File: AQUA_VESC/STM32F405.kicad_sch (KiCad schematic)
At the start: 15 parts, among them J3 Conn_01x05_Pin, U4 STM32F405RGTx, X1 8MHz

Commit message: AQUA VESC仮完成
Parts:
- renumbered U4 to U3
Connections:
- net ADC_EXT2 renamed MISO_ADC_EXT2
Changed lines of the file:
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@@
 		)
 	)
-	(hierarchical_label "ADC_EXT2"
+	(hierarchical_label "MISO_ADC_EXT2"
 		(shape output)
 		(at 80.01 53.34 0)
@@
 		(dnp no)
 		(fields_autoplaced yes)
-		(property "Reference" "#PWR029"
+		(property "Reference" "#PWR025"
 			(at 22.86 39.37 0)
 			(effects
@@
 			(project "AQUA_VESC"
 				(path "/8ee9fd02-9bd5-4905-927f-d8ca1179f479/d65f5897-766b-4e01-8d8f-d620c6f94f16"
-					(reference "#PWR029")
+					(reference "#PWR025")
 					(unit 1)
 				)
@@
 		(dnp no)
 		(fields_autoplaced yes)
-		(property "Reference" "#PWR031"
+		(property "Reference" "#PWR027"
 			(at 26.67 125.73 0)
 			(effects
@@
 			(project "AQUA_VESC"
 				(path "/8ee9fd02-9bd5-4905-927f-d8ca1179f479/d65f5897-766b-4e01-8d8f-d620c6f94f16"
-					(reference "#PWR031")
+					(reference "#PWR027")
 					(unit 1)
 				)
@@
 		(dnp no)
 		(fields_autoplaced yes)
-		(property "Reference" "#PWR036"
+		(property "Reference" "#PWR032"
 			(at 82.55 36.83 0)
 			(effects
@@
 			(project "AQUA_VESC"
 				(path "/8ee9fd02-9bd5-4905-927f-d8ca1179f479/d65f5897-766b-4e01-8d8f-d620c6f94f16"
-					(reference "#PWR036")
+					(reference "#PWR032")
 					(unit 1)
 				)
@@
 		(dnp no)
 		(fields_autoplaced yes)
-		(property "Reference" "#PWR030"
+		(property "Reference" "#PWR026"
 			(at 22.86 45.72 0)
 			(effects
@@
 			(project "AQUA_VESC"
 				(path "/8ee9fd02-9bd5-4905-927f-d8ca1179f479/d65f5897-766b-4e01-8d8f-d620c6f94f16"
-					(reference "#PWR030")
+					(reference "#PWR026")
 					(unit 1)
 				)
@@
 		(dnp no)
 		(fields_autoplaced yes)
-		(property "Reference" "#PWR038"
+		(property "Reference" "#PWR034"
 			(at 118.11 38.1 0)
 			(effects
@@
 			(project "AQUA_VESC"
 				(path "/8ee9fd02-9bd5-4905-927f-d8ca1179f479/d65f5897-766b-4e01-8d8f-d620c6f94f16"
-					(reference "#PWR038")
+					(reference "#PWR034")
 					(unit 1)
 				)
@@
 		(dnp no)
 		(fields_autoplaced yes)
-		(property "Reference" "U4"
+		(property "Reference" "U3"
 			(at 64.3733 127 0)
 			(effects
@@
 			(project ""
 				(path "/8ee9fd02-9bd5-4905-927f-d8ca1179f479/d65f5897-766b-4e01-8d8f-d620c6f94f16"
-					(reference "U4")
+					(reference "U3")
 					(unit 1)
 				)
@@
 		(dnp no)
 		(fields_autoplaced yes)
-		(property "Reference" "#PWR035"
+		(property "Reference" "#PWR031"
 			(at 67.31 22.86 0)
 			(effects
@@
 			(project ""
 				(path "/8ee9fd02-9bd5-4905-927f-d8ca1179f479/d65f5897-766b-4e01-8d8f-d620c6f94f16"
-					(reference "#PWR035")
+					(reference "#PWR031")
 					(unit 1)
 				)
@@
 		(dnp no)
 		(fields_autoplaced yes)
-		(property "Reference" "#PWR037"
+		(property "Reference" "#PWR033"
 			(at 120.65 33.02 0)
 			(effects
@@
 			(project "AQUA_VESC"
 				(path "/8ee9fd02-9bd5-4905-927f-d8ca1179f479/d65f5897-766b-4e01-8d8f-d620c6f94f16"
-					(reference "#PWR037")
+					(reference "#PWR033")
 					(unit 1)
 				)
@@
 		(dnp no)
 		(fields_autoplaced yes)
-		(property "Reference" "#PWR032"
+		(property "Reference" "#PWR028"
 			(at 27.94 67.31 0)
 			(effects
@@
 			(project "AQUA_VESC"
 				(path "/8ee9fd02-9bd5-4905-927f-d8ca1179f479/d65f5897-766b-4e01-8d8f-d620c6f94f16"
-					(reference "#PWR032")
+					(reference "#PWR028")
 					(unit 1)
 				)
@@
 		(dnp no)
 		(fields_autoplaced yes)
-		(property "Reference" "#PWR027"
+		(property "Reference" "#PWR023"
 			(at 17.78 67.31 0)
 			(effects
@@
 			(project "AQUA_VESC"
 				(path "/8ee9fd02-9bd5-4905-927f-d8ca1179f479/d65f5897-766b-4e01-8d8f-d620c6f94f16"
-					(reference "#PWR027")
+					(reference "#PWR023")
 					(unit 1)
 				)
@@
 		(dnp no)
 		(fields_autoplaced yes)
-		(property "Reference" "#PWR033"
+		(property "Reference" "#PWR029"
 			(at 31.75 49.53 0)
 			(effects
@@
 			(project "AQUA_VESC"
 				(path "/8ee9fd02-9bd5-4905-927f-d8ca1179f479/d65f5897-766b-4e01-8d8f-d620c6f94f16"
-					(reference "#PWR033")
+					(reference "#PWR029")
 					(unit 1)
 				)
@@
 		(dnp no)
 		(fields_autoplaced yes)
-		(property "Reference" "#PWR034"
+		(property "Reference" "#PWR030"
 			(at 59.69 135.89 0)
 			(effects
@@
 			(project ""
 				(path "/8ee9fd02-9bd5-4905-927f-d8ca1179f479/d65f5897-766b-4e01-8d8f-d620c6f94f16"
-					(reference "#PWR034")
+					(reference "#PWR030")
 					(unit 1)
 				)
@@
 		(dnp no)
 		(fields_autoplaced yes)
-		(property "Reference" "#PWR028"
+		(property "Reference" "#PWR024"
 			(at 22.86 22.86 0)
 			(effects
@@
 			(project "AQUA_VESC"
 				(path "/8ee9fd02-9bd5-4905-927f-d8ca1179f479/d65f5897-766b-4e01-8d8f-d620c6f94f16"
-					(reference "#PWR028")
-					(unit 1)
-				)
+					(reference "#PWR024")
+					(unit 1)
+				)

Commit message: 制御基板REV01完成
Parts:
- renumbered J3 to J2
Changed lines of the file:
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@@
 		(dnp no)
 		(fields_autoplaced yes)
-		(property "Reference" "#PWR025"
+		(property "Reference" "#PWR024"
 			(at 22.86 39.37 0)
 			(effects
@@
 			(project "AQUA_VESC"
 				(path "/8ee9fd02-9bd5-4905-927f-d8ca1179f479/d65f5897-766b-4e01-8d8f-d620c6f94f16"
-					(reference "#PWR025")
+					(reference "#PWR024")
 					(unit 1)
 				)
@@
 		(dnp no)
 		(fields_autoplaced yes)
-		(property "Reference" "J3"
+		(property "Reference" "J2"
 			(at 134.62 36.8299 0)
 			(effects
@@
 			(project ""
 				(path "/8ee9fd02-9bd5-4905-927f-d8ca1179f479/d65f5897-766b-4e01-8d8f-d620c6f94f16"
-					(reference "J3")
+					(reference "J2")
 					(unit 1)
 				)
@@
 		(dnp no)
 		(fields_autoplaced yes)
-		(property "Reference" "#PWR027"
+		(property "Reference" "#PWR026"
 			(at 26.67 125.73 0)
 			(effects
@@
 			(project "AQUA_VESC"
 				(path "/8ee9fd02-9bd5-4905-927f-d8ca1179f479/d65f5897-766b-4e01-8d8f-d620c6f94f16"
-					(reference "#PWR027")
+					(reference "#PWR026")
 					(unit 1)
 				)
@@
 		(dnp no)
 		(fields_autoplaced yes)
-		(property "Reference" "#PWR032"
+		(property "Reference" "#PWR031"
 			(at 82.55 36.83 0)
 			(effects
@@
 			(project "AQUA_VESC"
 				(path "/8ee9fd02-9bd5-4905-927f-d8ca1179f479/d65f5897-766b-4e01-8d8f-d620c6f94f16"
-					(reference "#PWR032")
+					(reference "#PWR031")
 					(unit 1)
 				)
@@
 		(dnp no)
 		(fields_autoplaced yes)
-		(property "Reference" "#PWR026"
+		(property "Reference" "#PWR025"
 			(at 22.86 45.72 0)
 			(effects
@@
 			(project "AQUA_VESC"
 				(path "/8ee9fd02-9bd5-4905-927f-d8ca1179f479/d65f5897-766b-4e01-8d8f-d620c6f94f16"
-					(reference "#PWR026")
+					(reference "#PWR025")
 					(unit 1)
 				)
@@
 		(dnp no)
 		(fields_autoplaced yes)
-		(property "Reference" "#PWR034"
+		(property "Reference" "#PWR033"
 			(at 118.11 38.1 0)
 			(effects
@@
 			(project "AQUA_VESC"
 				(path "/8ee9fd02-9bd5-4905-927f-d8ca1179f479/d65f5897-766b-4e01-8d8f-d620c6f94f16"
-					(reference "#PWR034")
+					(reference "#PWR033")
 					(unit 1)
 				)
@@
 		(dnp no)
 		(fields_autoplaced yes)
-		(property "Reference" "#PWR031"
+		(property "Reference" "#PWR030"
 			(at 67.31 22.86 0)
 			(effects
@@
 			(project ""
 				(path "/8ee9fd02-9bd5-4905-927f-d8ca1179f479/d65f5897-766b-4e01-8d8f-d620c6f94f16"
-					(reference "#PWR031")
+					(reference "#PWR030")
 					(unit 1)
 				)
@@
 		(dnp no)
 		(fields_autoplaced yes)
-		(property "Reference" "#PWR033"
+		(property "Reference" "#PWR032"
 			(at 120.65 33.02 0)
 			(effects
@@
 			(project "AQUA_VESC"
 				(path "/8ee9fd02-9bd5-4905-927f-d8ca1179f479/d65f5897-766b-4e01-8d8f-d620c6f94f16"
-					(reference "#PWR033")
+					(reference "#PWR032")
 					(unit 1)
 				)
@@
 		(dnp no)
 		(fields_autoplaced yes)
-		(property "Reference" "#PWR028"
+		(property "Reference" "#PWR027"
 			(at 27.94 67.31 0)
 			(effects
@@
 			(project "AQUA_VESC"
 				(path "/8ee9fd02-9bd5-4905-927f-d8ca1179f479/d65f5897-766b-4e01-8d8f-d620c6f94f16"
-					(reference "#PWR028")
+					(reference "#PWR027")
 					(unit 1)
 				)
@@
 		(dnp no)
 		(fields_autoplaced yes)
-		(property "Reference" "#PWR023"
+		(property "Reference" "#PWR022"
 			(at 17.78 67.31 0)
 			(effects
@@
 			(project "AQUA_VESC"
 				(path "/8ee9fd02-9bd5-4905-927f-d8ca1179f479/d65f5897-766b-4e01-8d8f-d620c6f94f16"
-					(reference "#PWR023")
+					(reference "#PWR022")
 					(unit 1)
 				)
@@
 		(dnp no)
 		(fields_autoplaced yes)
-		(property "Reference" "#PWR029"
+		(property "Reference" "#PWR028"
 			(at 31.75 49.53 0)
 			(effects
@@
 			(project "AQUA_VESC"
 				(path "/8ee9fd02-9bd5-4905-927f-d8ca1179f479/d65f5897-766b-4e01-8d8f-d620c6f94f16"
-					(reference "#PWR029")
+					(reference "#PWR028")
 					(unit 1)
 				)
@@
 		(dnp no)
 		(fields_autoplaced yes)
-		(property "Reference" "#PWR030"
+		(property "Reference" "#PWR029"
 			(at 59.69 135.89 0)
 			(effects
@@
 			(project ""
 				(path "/8ee9fd02-9bd5-4905-927f-d8ca1179f479/d65f5897-766b-4e01-8d8f-d620c6f94f16"
-					(reference "#PWR030")
+					(reference "#PWR029")
 					(unit 1)
 				)
@@
 		(dnp no)
 		(fields_autoplaced yes)
-		(property "Reference" "#PWR024"
+		(property "Reference" "#PWR023"
 			(at 22.86 22.86 0)
 			(effects
@@
 			(project "AQUA_VESC"
 				(path "/8ee9fd02-9bd5-4905-927f-d8ca1179f479/d65f5897-766b-4e01-8d8f-d620c6f94f16"
-					(reference "#PWR024")
-					(unit 1)
-				)
+					(reference "#PWR023")
+					(unit 1)
+				)

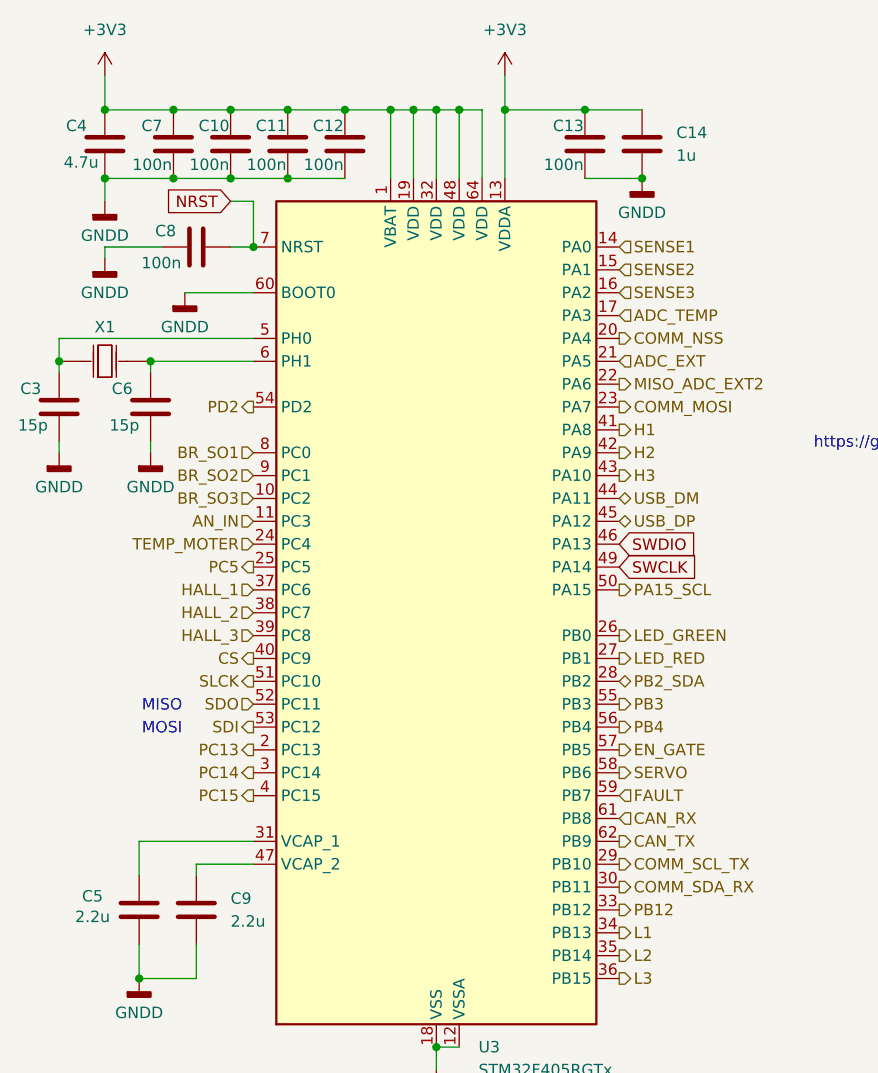
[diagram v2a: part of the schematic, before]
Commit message: 方針変更、back_connector_escにMT60を使用しないことに
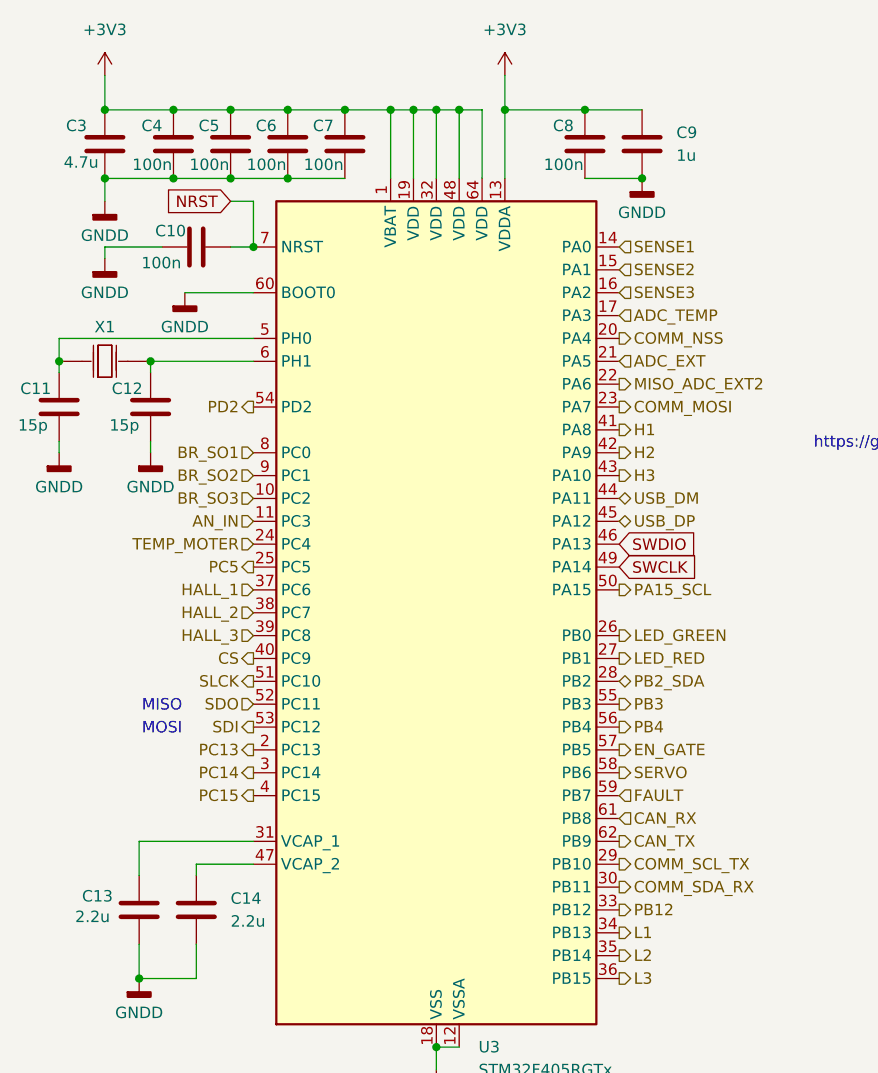
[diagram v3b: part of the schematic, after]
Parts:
- renumbered C8 to C10, C3 to C11, C6 to C12, C5 to C13, C9 to C14, C4 to C3, C7 to C4, C10 to C5, C11 to C6, C12 to C7, C13 to C8, C14 to C9
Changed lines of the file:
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@@
 		(dnp no)
 		(fields_autoplaced yes)
-		(property "Reference" "#PWR024"
+		(property "Reference" "#PWR032"
 			(at 22.86 39.37 0)
 			(effects
@@
 			(project "AQUA_VESC"
 				(path "/8ee9fd02-9bd5-4905-927f-d8ca1179f479/d65f5897-766b-4e01-8d8f-d620c6f94f16"
-					(reference "#PWR024")
+					(reference "#PWR032")
 					(unit 1)
 				)
@@
 		(on_board yes)
 		(dnp no)
-		(property "Reference" "C13"
+		(property "Reference" "C8"
 			(at 72.644 24.638 0)
 			(effects
@@
 			(project "AQUA_VESC"
 				(path "/8ee9fd02-9bd5-4905-927f-d8ca1179f479/d65f5897-766b-4e01-8d8f-d620c6f94f16"
-					(reference "C13")
+					(reference "C8")
 					(unit 1)
 				)
@@
 		(on_board yes)
 		(dnp no)
-		(property "Reference" "C8"
+		(property "Reference" "C10"
 			(at 28.448 36.322 90)
 			(effects
@@
 			(project ""
 				(path "/8ee9fd02-9bd5-4905-927f-d8ca1179f479/d65f5897-766b-4e01-8d8f-d620c6f94f16"
-					(reference "C8")
+					(reference "C10")
 					(unit 1)
 				)
@@
 		(on_board yes)
 		(dnp no)
-		(property "Reference" "C11"
+		(property "Reference" "C6"
 			(at 39.624 24.638 0)
 			(effects
@@
 			(project "AQUA_VESC"
 				(path "/8ee9fd02-9bd5-4905-927f-d8ca1179f479/d65f5897-766b-4e01-8d8f-d620c6f94f16"
-					(reference "C11")
+					(reference "C6")
 					(unit 1)
 				)
@@
 		(dnp no)
 		(fields_autoplaced yes)
-		(property "Reference" "#PWR026"
+		(property "Reference" "#PWR038"
 			(at 26.67 125.73 0)
 			(effects
@@
 			(project "AQUA_VESC"
 				(path "/8ee9fd02-9bd5-4905-927f-d8ca1179f479/d65f5897-766b-4e01-8d8f-d620c6f94f16"
-					(reference "#PWR026")
+					(reference "#PWR038")
 					(unit 1)
 				)
@@
 		(dnp no)
 		(fields_autoplaced yes)
-		(property "Reference" "#PWR025"
+		(property "Reference" "#PWR034"
 			(at 22.86 45.72 0)
 			(effects
@@
 			(project "AQUA_VESC"
 				(path "/8ee9fd02-9bd5-4905-927f-d8ca1179f479/d65f5897-766b-4e01-8d8f-d620c6f94f16"
-					(reference "#PWR025")
+					(reference "#PWR034")
 					(unit 1)
 				)
@@
 		(on_board yes)
 		(dnp no)
-		(property "Reference" "C10"
+		(property "Reference" "C5"
 			(at 33.274 24.638 0)
 			(effects
@@
 			(project "AQUA_VESC"
 				(path "/8ee9fd02-9bd5-4905-927f-d8ca1179f479/d65f5897-766b-4e01-8d8f-d620c6f94f16"
-					(reference "C10")
+					(reference "C5")
 					(unit 1)
 				)
@@
 		(dnp no)
 		(fields_autoplaced yes)
-		(property "Reference" "#PWR030"
+		(property "Reference" "#PWR029"
 			(at 67.31 22.86 0)
 			(effects
@@
 			(project ""
 				(path "/8ee9fd02-9bd5-4905-927f-d8ca1179f479/d65f5897-766b-4e01-8d8f-d620c6f94f16"
-					(reference "#PWR030")
+					(reference "#PWR029")
 					(unit 1)
 				)
@@
 		(on_board yes)
 		(dnp no)
-		(property "Reference" "C7"
+		(property "Reference" "C4"
 			(at 26.924 24.638 0)
 			(effects
@@
 			(project "AQUA_VESC"
 				(path "/8ee9fd02-9bd5-4905-927f-d8ca1179f479/d65f5897-766b-4e01-8d8f-d620c6f94f16"
-					(reference "C7")
+					(reference "C4")
 					(unit 1)
 				)
@@
 		(dnp no)
 		(fields_autoplaced yes)
-		(property "Reference" "#PWR032"
+		(property "Reference" "#PWR030"
 			(at 120.65 33.02 0)
 			(effects
@@
 			(project "AQUA_VESC"
 				(path "/8ee9fd02-9bd5-4905-927f-d8ca1179f479/d65f5897-766b-4e01-8d8f-d620c6f94f16"
-					(reference "#PWR032")
+					(reference "#PWR030")
 					(unit 1)
 				)
@@
 		(dnp no)
 		(fields_autoplaced yes)
-		(property "Reference" "#PWR027"
+		(property "Reference" "#PWR037"
 			(at 27.94 67.31 0)
 			(effects
@@
 			(project "AQUA_VESC"
 				(path "/8ee9fd02-9bd5-4905-927f-d8ca1179f479/d65f5897-766b-4e01-8d8f-d620c6f94f16"
-					(reference "#PWR027")
+					(reference "#PWR037")
 					(unit 1)
 				)
@@
 		(dnp no)
 		(fields_autoplaced yes)
-		(property "Reference" "#PWR022"
+		(property "Reference" "#PWR036"
 			(at 17.78 67.31 0)
 			(effects
@@
 			(project "AQUA_VESC"
 				(path "/8ee9fd02-9bd5-4905-927f-d8ca1179f479/d65f5897-766b-4e01-8d8f-d620c6f94f16"
-					(reference "#PWR022")
+					(reference "#PWR036")
 					(unit 1)
 				)
@@
 		(on_board yes)
 		(dnp no)
-		(property "Reference" "C5"
+		(property "Reference" "C13"
 			(at 20.32 110.236 0)
 			(effects
@@
 			(project "AQUA_VESC"
 				(path "/8ee9fd02-9bd5-4905-927f-d8ca1179f479/d65f5897-766b-4e01-8d8f-d620c6f94f16"
-					(reference "C5")
+					(reference "C13")
 					(unit 1)
 				)
@@
 		(dnp no)
 		(fields_autoplaced yes)
-		(property "Reference" "C14"
+		(property "Reference" "C9"
 			(at 86.36 25.3999 0)
 			(effects
@@
 			(project "AQUA_VESC"
 				(path "/8ee9fd02-9bd5-4905-927f-d8ca1179f479/d65f5897-766b-4e01-8d8f-d620c6f94f16"
-					(reference "C14")
+					(reference "C9")
 					(unit 1)
 				)
@@
 		(dnp no)
 		(fields_autoplaced yes)
-		(property "Reference" "#PWR028"
+		(property "Reference" "#PWR035"
 			(at 31.75 49.53 0)
 			(effects
@@
 			(project "AQUA_VESC"
 				(path "/8ee9fd02-9bd5-4905-927f-d8ca1179f479/d65f5897-766b-4e01-8d8f-d620c6f94f16"
-					(reference "#PWR028")
+					(reference "#PWR035")
 					(unit 1)
 				)
@@
 		(dnp no)
 		(fields_autoplaced yes)
-		(property "Reference" "#PWR029"
+		(property "Reference" "#PWR039"
 			(at 59.69 135.89 0)
 			(effects
@@
 			(project ""
 				(path "/8ee9fd02-9bd5-4905-927f-d8ca1179f479/d65f5897-766b-4e01-8d8f-d620c6f94f16"
-					(reference "#PWR029")
+					(reference "#PWR039")
 					(unit 1)
 				)
@@
 		(on_board yes)
 		(dnp no)
-		(property "Reference" "C12"
+		(property "Reference" "C7"
 			(at 45.974 24.638 0)
 			(effects
@@
 			(project "AQUA_VESC"
 				(path "/8ee9fd02-9bd5-4905-927f-d8ca1179f479/d65f5897-766b-4e01-8d8f-d620c6f94f16"
-					(reference "C12")
+					(reference "C7")
 					(unit 1)
 				)
@@
 		(dnp no)
 		(fields_autoplaced yes)
-		(property "Reference" "#PWR023"
+		(property "Reference" "#PWR028"
 			(at 22.86 22.86 0)
 			(effects
@@
 			(project "AQUA_VESC"
 				(path "/8ee9fd02-9bd5-4905-927f-d8ca1179f479/d65f5897-766b-4e01-8d8f-d620c6f94f16"
-					(reference "#PWR023")
+					(reference "#PWR028")
 					(unit 1)
 				)
@@
 		(on_board yes)
 		(dnp no)
-		(property "Reference" "C3"
+		(property "Reference" "C11"
 			(at 13.462 53.848 0)
 			(effects
@@
 			(project "AQUA_VESC"
 				(path "/8ee9fd02-9bd5-4905-927f-d8ca1179f479/d65f5897-766b-4e01-8d8f-d620c6f94f16"
-					(reference "C3")
+					(reference "C11")
 					(unit 1)
 				)
@@
 		(on_board yes)
 		(dnp no)
-		(property "Reference" "C4"
+		(property "Reference" "C3"
 			(at 18.542 24.638 0)
 			(effects
@@
 			(project "AQUA_VESC"
 				(path "/8ee9fd02-9bd5-4905-927f-d8ca1179f479/d65f5897-766b-4e01-8d8f-d620c6f94f16"
-					(reference "C4")
+					(reference "C3")
 					(unit 1)
 				)
@@
 		(dnp no)
 		(fields_autoplaced yes)
-		(property "Reference" "C9"
+		(property "Reference" "C14"
 			(at 36.83 110.4899 0)
 			(effects
@@
 			(project "AQUA_VESC"
 				(path "/8ee9fd02-9bd5-4905-927f-d8ca1179f479/d65f5897-766b-4e01-8d8f-d620c6f94f16"
-					(reference "C9")
+					(reference "C14")
 					(unit 1)
 				)
@@
 		(on_board yes)
 		(dnp no)
-		(property "Reference" "C6"
+		(property "Reference" "C12"
 			(at 23.622 53.848 0)
 			(effects
@@
 			(project "AQUA_VESC"
 				(path "/8ee9fd02-9bd5-4905-927f-d8ca1179f479/d65f5897-766b-4e01-8d8f-d620c6f94f16"
-					(reference "C6")
-					(unit 1)
-				)
+					(reference "C12")
+					(unit 1)
+				)
